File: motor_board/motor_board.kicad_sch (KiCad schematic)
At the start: 15 parts, among them J1 Conn_01x02_Socket, J2 Conn_01x02_Socket, J3 Conn_01x08_Socket, U1 DRV8833PW, U2 DCP3603BCMR

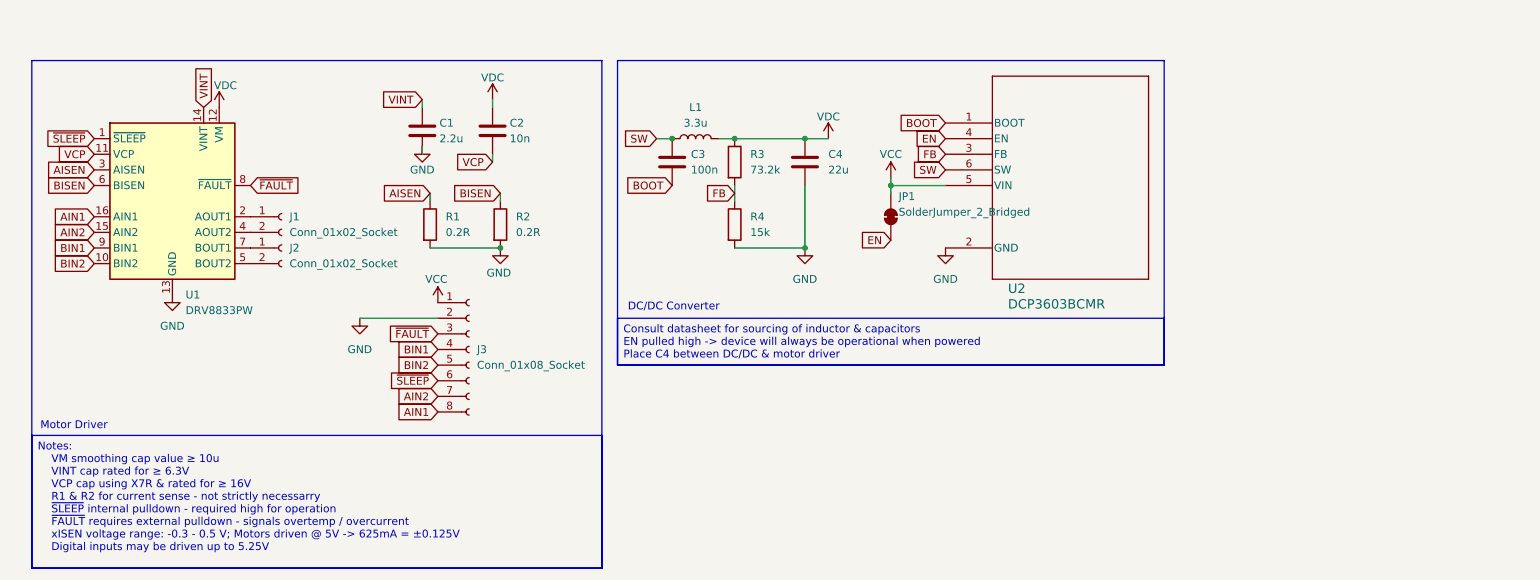
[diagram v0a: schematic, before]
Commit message: Added TODO for motor_board
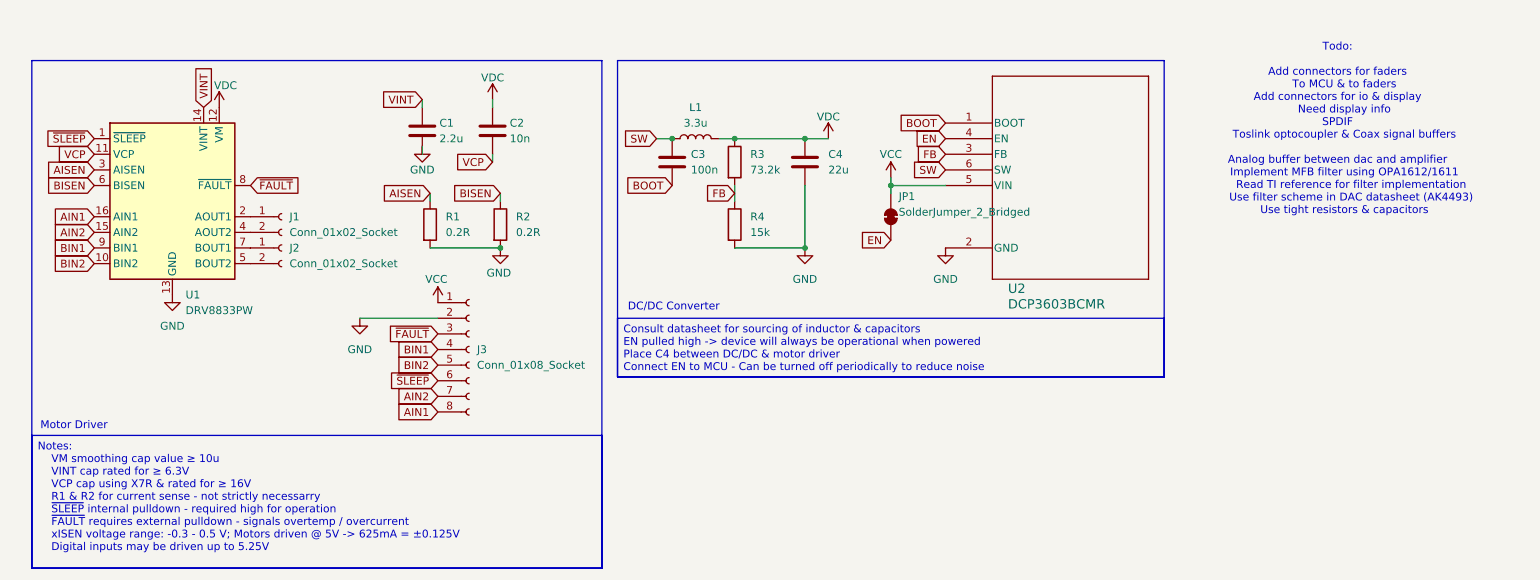
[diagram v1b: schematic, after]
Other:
- note added: "Todo: Add connectors for faders To MCU & to faders Add connectors for io & display Need display info SPDIF Toslink optocoupler & Coax signal buffers Analog buffer between dac and amplifier Implement MFB filter using OPA1612/1611 Read TI reference for filter implementation Use filter scheme in DAC datasheet (AK4493) Use tight resistors & capacitors"
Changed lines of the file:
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@@
 	(rectangle
 		(start 115.57 25.4)
-		(end 204.47 74.93)
+		(end 204.47 76.835)
 		(stroke
 			(width 0)
@@
 		)
 	)
+	(text "Todo:\n\nAdd connectors for faders\n	To MCU & to faders\nAdd connectors for io & display\n	Need display info\nSPDIF\n	Toslink optocoupler & Coax signal buffers\n\nAnalog buffer between dac and amplifier\n	Implement MFB filter using OPA1612/1611\n		Read TI reference for filter implementation\n		Use filter scheme in DAC datasheet (AK4493)\n	Use tight resistors & capacitors\n		"
+		(exclude_from_sim no)
+		(at 232.664 37.592 0)
+		(effects
+			(font
+				(size 1.27 1.27)
+			)
+		)
+	)
 	(text_box "Notes:\n	VM smoothing cap value ≥ 10u\n	VINT cap rated for ≥ 6.3V\n	VCP cap using X7R & rated for ≥ 16V\n	R1 & R2 for current sense - not strictly necessarry \n	~{SLEEP} internal pulldown - required high for operation\n	~{FAULT} requires external pulldown - signals overtemp / overcurrent\n	xISEN voltage range: -0.3 - 0.5 V; Motors driven @ 5V -> 625mA = ±0.125V\n	Digital inputs may be driven up to 5.25V"
 		(exclude_from_sim no)
@@
 		)
 	)
-	(text_box "Consult datasheet for sourcing of inductor & capacitors\nEN pulled high -> device will always be operational when powered\nPlace C4 between DC/DC & motor driver"
+	(text_box "Consult datasheet for sourcing of inductor & capacitors\nEN pulled high -> device will always be operational when powered\nPlace C4 between DC/DC & motor driver\nConnect EN to MCU - Can be turned off periodically to reduce noise\n"
 		(exclude_from_sim no)
 		(at 115.57 67.31 0)
-		(size 88.9 7.62)
+		(size 88.9 9.525)
 		(margins 0.9525 0.9525 0.9525 0.9525)
 		(stroke

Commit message: Finished motor_board & added SPDIF
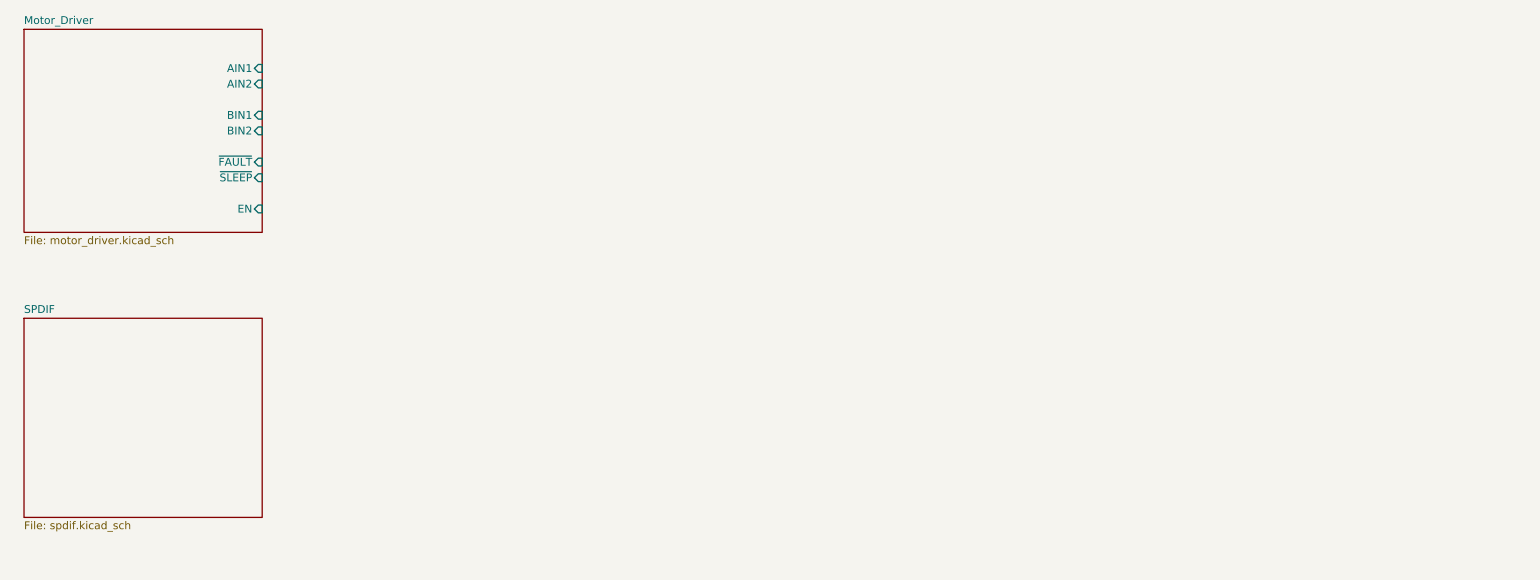
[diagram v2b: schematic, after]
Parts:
- removed C1: 2.2u, symbol Device:C
- removed C2: 10n, symbol Device:C
- removed C3: 100n, symbol Device:C
- removed C4: 22u, symbol Device:C
- removed J1, J2: Conn_01x02_Socket, Connector_JST:JST_PH_B2B-PH-K_1x02_P2.00mm_Vertical, symbol Connector:Conn_01x02_Socket
- removed J3: Conn_01x08_Socket, Connector_JST:JST_PH_B8B-PH-K_1x08_P2.00mm_Vertical, symbol Connector:Conn_01x08_Socket
- removed JP1: SolderJumper_2_Bridged, Jumper:SolderJumper-2_P1.3mm_Bridged_RoundedPad1.0x1.5mm, symbol Jumper:SolderJumper_2_Bridged
- removed L1: 3.3u, symbol Device:L
- removed R1, R2: 0.2R, symbol Device:R
- removed R3: 73.2k, Resistor_SMD:R_0402_1005Metric_Pad0.72x0.64mm_HandSolder, symbol Device:R
- removed R4: 15k, Resistor_SMD:R_0402_1005Metric_Pad0.72x0.64mm_HandSolder, symbol Device:R
- removed U1: DRV8833PW, Package_SO:TSSOP-16_4.4x5mm_P0.65mm, symbol Driver_Motor:DRV8833PW
- removed U2: DCP3603BCMR, footprints:SOT23-6L_1p7x3p01_STM, symbol 2026-02-10_02-42-14:DCP3603BCMR
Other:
- added sheet Motor_Driver (motor_driver.kicad_sch)
- added sheet SPDIF (spdif.kicad_sch)
- note removed: "DC/DC Converter"
- note removed: "Motor Driver"
- note removed: "Todo: Add connectors for faders To MCU & to faders Add connectors for io & display Need display info SPDIF Toslink optocoupler & Coax signal buffers Analog buffer between dac and amplifier Implement MFB filter using OPA1612/1611 Read TI reference for filter implementation Use filter scheme in DAC datasheet (AK4493) Use tight resistors & capacitors"

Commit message: Began motor board layour
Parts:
- added H1, H2, H3, H4: MountingHole, MountingHole:MountingHole_3.2mm_M3, symbol Mechanical:MountingHole
- added J1: Conn_01x16_Socket, Connector_JST:JST_PH_S16B-PH-K_1x16_P2.00mm_Horizontal, symbol Connector:Conn_01x16_Socket
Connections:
- new net +3.3V: J1.14 (Pin_14)
- new net +5V: J1.15 (Pin_15)
- new net AIN1: J1.1 (Pin_1)
- new net AIN2: J1.2 (Pin_2)
- new net BIN1: J1.3 (Pin_3)
- new net BIN2: J1.4 (Pin_4)
- new net EN: J1.7 (Pin_7)
- new net GND: J1.12 (Pin_12)
- new net GNDD: J1.13 (Pin_13)
- new net SPDIFRX_COAX: J1.10 (Pin_10)
- new net SPDIFRX_TOS: J1.11 (Pin_11)
- new net VCC: J1.16 (Pin_16)
- new net WIPER_A: J1.8 (Pin_8)
- new net WIPER_B: J1.9 (Pin_9)
- new net ~{FAULT}: J1.5 (Pin_5)
- new net ~{SLEEP}: J1.6 (Pin_6)
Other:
- sheet Motor_Driver ports: added WIPER_A, WIPER_B; removed none
- sheet SPDIF ports: added SPDIFRX_COAX, SPDIFRX_TOS; removed none

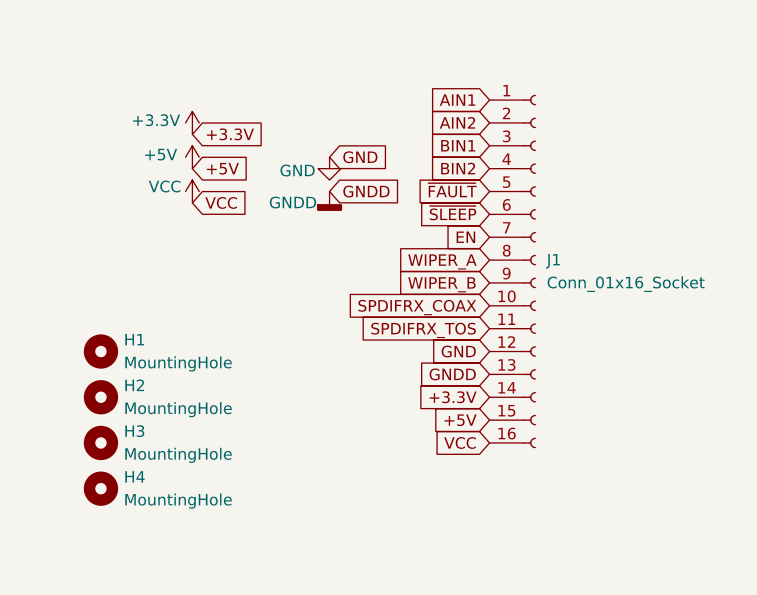
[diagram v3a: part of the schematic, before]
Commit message: Finished motor board PCB
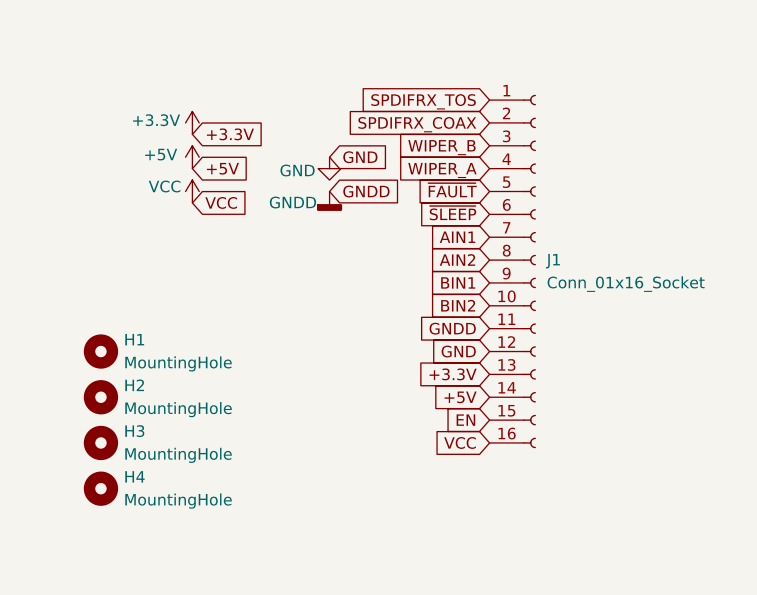
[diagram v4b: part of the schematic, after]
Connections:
- net +3.3V: now also J1.13 (Pin_13); no longer J1.14 (Pin_14)
- net +5V: now also J1.14 (Pin_14); no longer J1.15 (Pin_15)
- net AIN1: now also J1.7 (Pin_7); no longer J1.1 (Pin_1)
- net AIN2: now also J1.8 (Pin_8); no longer J1.2 (Pin_2)
- net BIN1: now also J1.9 (Pin_9); no longer J1.3 (Pin_3)
- net BIN2: now also J1.10 (Pin_10); no longer J1.4 (Pin_4)
- net EN: now also J1.15 (Pin_15); no longer J1.7 (Pin_7)
- net GNDD: now also J1.11 (Pin_11); no longer J1.13 (Pin_13)
- net SPDIFRX_COAX: now also J1.2 (Pin_2); no longer J1.10 (Pin_10)
- net SPDIFRX_TOS: now also J1.1 (Pin_1); no longer J1.11 (Pin_11)
- net WIPER_A: now also J1.4 (Pin_4); no longer J1.8 (Pin_8)
- net WIPER_B: now also J1.3 (Pin_3); no longer J1.9 (Pin_9)
